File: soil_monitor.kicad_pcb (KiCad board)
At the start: 2 copper layers, 81 x 98 mm, 48 parts, among them J1 Conn_01x02_Male, J2 Conn_01x02_Male, J3 Conn_01x02_Male, J4 Conn_01x04_Male, J5 Conn_01x04_Male, J6 Conn_01x04_Male, U1 TL072, U2 TL072, U3 TL072

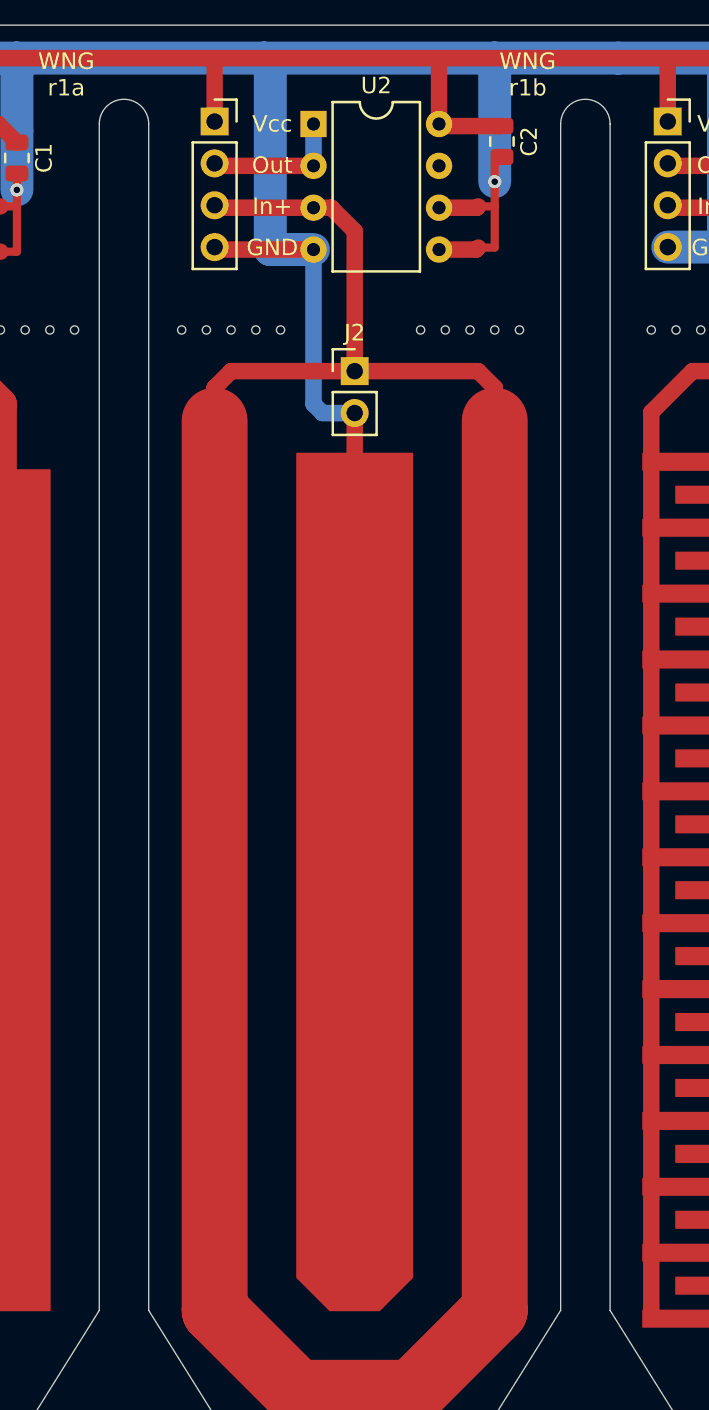
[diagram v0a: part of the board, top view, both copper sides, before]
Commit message: added mouses bites, packaged files for fab
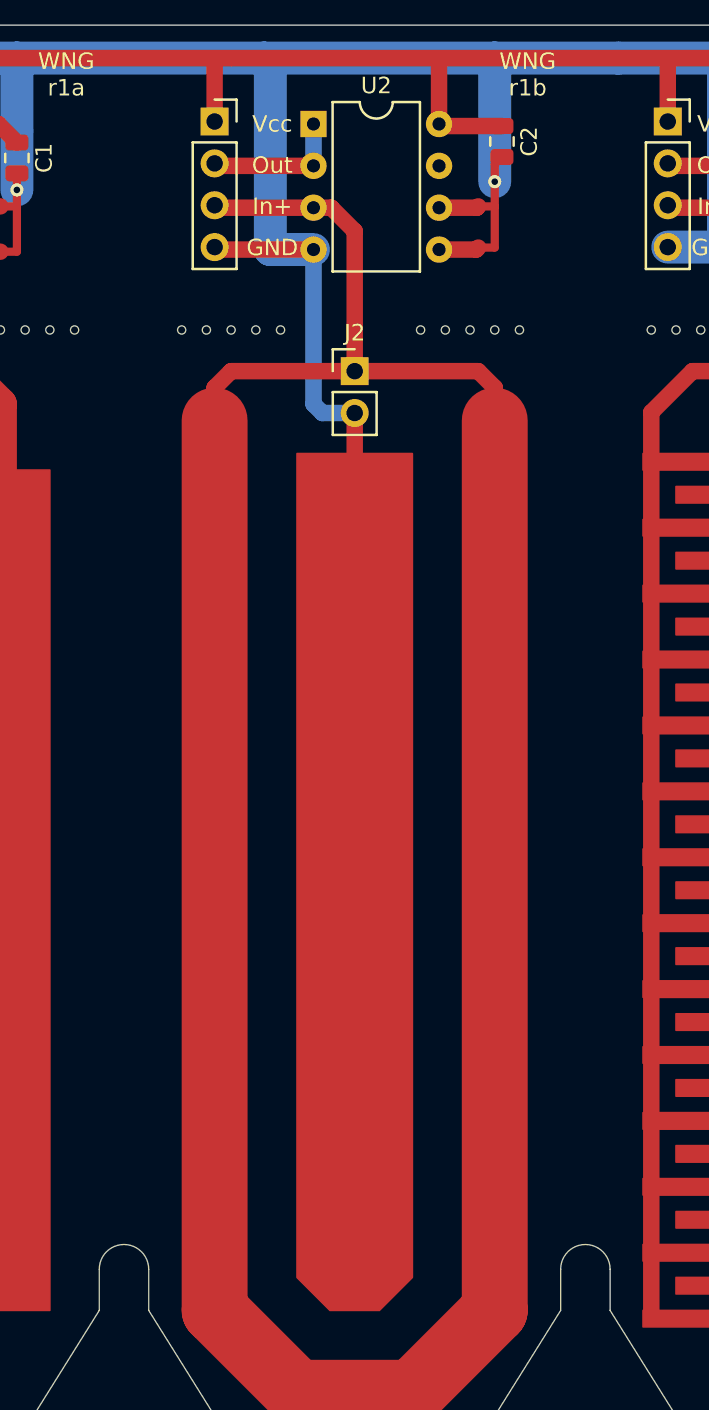
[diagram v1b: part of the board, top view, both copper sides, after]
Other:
- outline, holes or cut-outs redrawn
